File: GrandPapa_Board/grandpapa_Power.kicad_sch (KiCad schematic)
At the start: 44 parts, among them J10 Conn_01x03_Female, J7 Conn_01x02_Female, J8 Conn_01x02_Female, J9 Conn_01x02_Female, Q1 NMOS_SDG, Q2 PMOS_SDG, U1 LD2985BM33R, U2 INA180A4QDBVRQ1, U3 INA180A4QDBVRQ1, U4 LT1576IS8-5#TRPBF, U5 FPF2124, U9 INA180A4QDBVRQ1

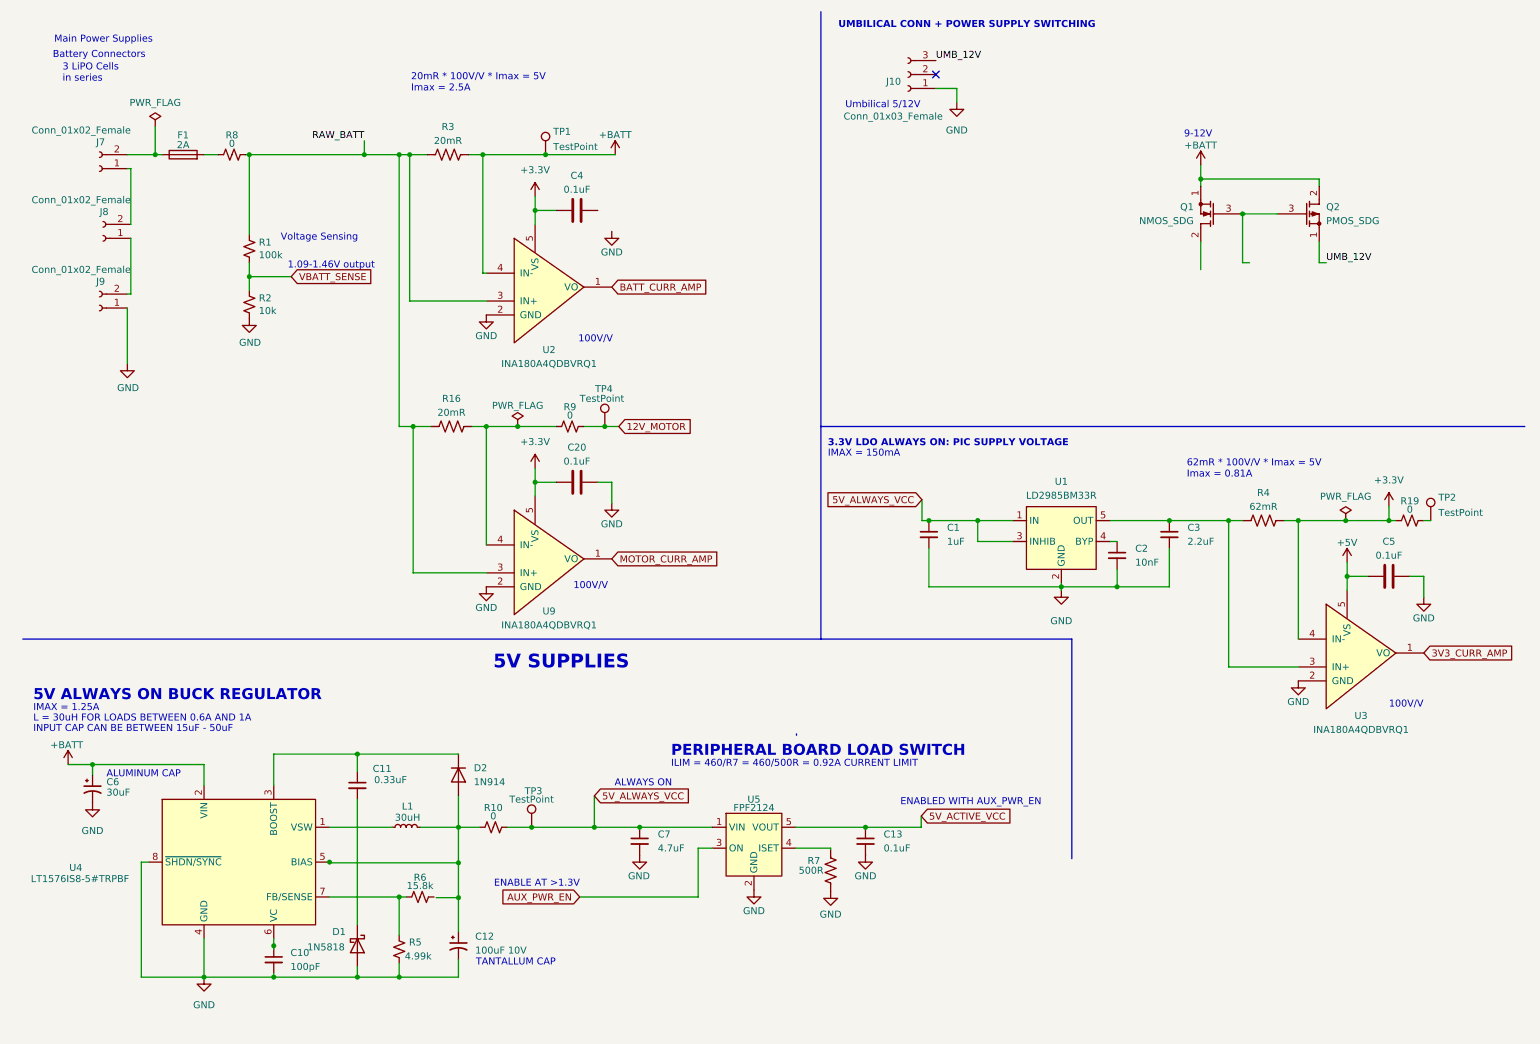
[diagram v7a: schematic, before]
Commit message: Remove 3.3V, placeholders for battery charge IC and 5V boost converter
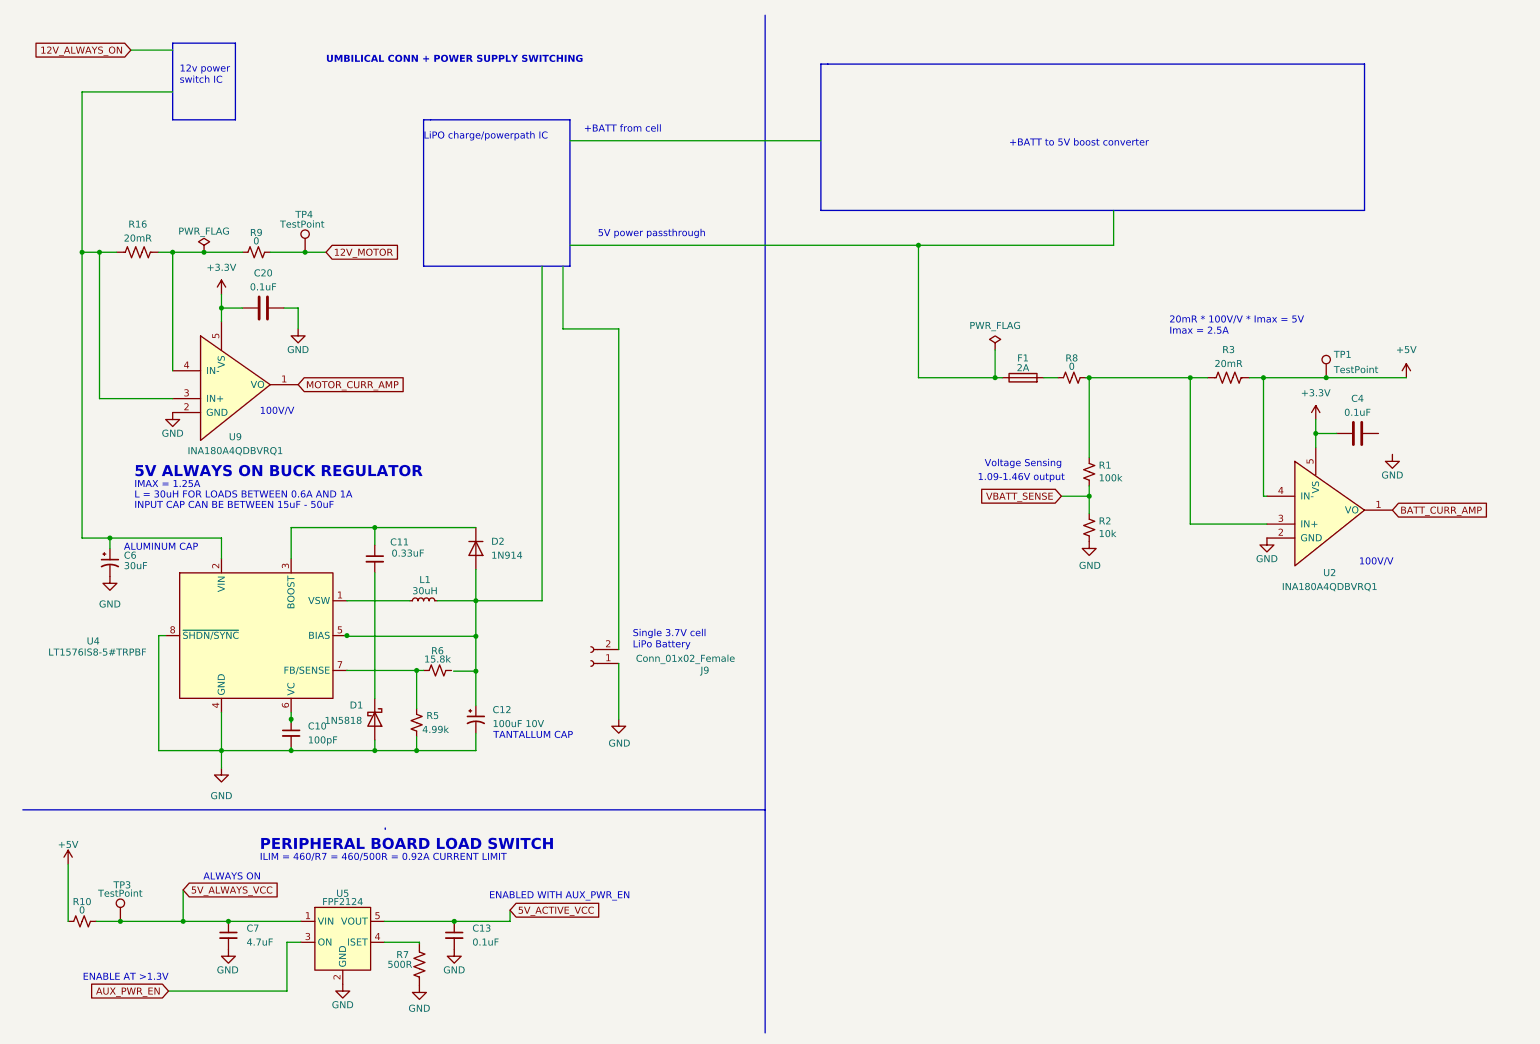
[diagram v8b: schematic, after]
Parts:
- removed C1: 1uF, symbol Device:C_Small
- removed C2: 10nF, symbol Device:C_Small
- removed C3: 2.2uF, symbol Device:C_Small
- removed C5: 0.1uF, Capacitor_SMD:C_0805_2012Metric_Pad1.18x1.45mm_HandSolder, symbol Device:C
- removed J10: Conn_01x03_Female, symbol Connector:Conn_01x03_Female
- removed J7, J8: Conn_01x02_Female, Connector_JST:JST_PH_S2B-PH-K_1x02_P2.00mm_Horizontal, symbol Connector:Conn_01x02_Female
- removed Q1: NMOS_SDG, symbol CLEAN_MOS:NMOS_SDG
- removed Q2: PMOS_SDG, symbol CLEAN_MOS:PMOS_SDG
- removed R19: 0, symbol Device:R_Small_US
- removed R4: 62mR, Resistor_SMD:R_1206_3216Metric_Pad1.30x1.75mm_HandSolder, symbol Device:R_US
- removed TP2: TestPoint, Connector_PinHeader_2.54mm:PinHeader_1x01_P2.54mm_Vertical, symbol Connector:TestPoint
- removed U1: LD2985BM33R, symbol grandpapa board:LD2985BM33R
- removed U3: INA180A4QDBVRQ1, Package_TO_SOT_SMD:SOT-23-5_HandSoldering, symbol payload2020_custom:INA180
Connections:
- net +5V: now also R10.1, R3.1, TP1.1, U2.4 (IN-)
- net at C12.1, D2.2 (A), L1.2: no longer R10.1
- removed net +BATT: C6.1, R3.1, TP1.1, U2.4 (IN-), U4.2 (VIN)
- net RAW_BATT: no longer names the net of R1.1, R3.2, R8.2, U2.3 (IN+)
- net RAW_BATT: no longer R16.2, U9.3 (IN+)
- new net: C6.1, R16.2, U4.2 (VIN), U9.3 (IN+)
- no-connect marks 1 -> 0
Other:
- note added: "+BATT from cell"
- note added: "+BATT to 5V boost converter"
- note added: "12v power switch IC"
- note added: "5V power passthrough"
- note added: "LiPO charge/powerpath IC"
- note added: "Single 3.7V cell LiPo Battery"
- note removed: "3 LiPO Cells in series"
- note removed: "3.3V LDO ALWAYS ON: PIC SUPPLY VOLTAGE"
- note removed: "5V SUPPLIES"
- note removed: "62mR * 100V/V * Imax = 5V Imax = 0.81A"
- note removed: "9-12V"
- note removed: "Battery Connectors"
- note removed: "IMAX = 150mA"
- note removed: "Main Power Supplies"
- note removed: "Umbilical 5/12V"
- moved on the sheet: C10, C11, C12, C13, C20, C4, C6, C7, D1, D2, F1, J9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
